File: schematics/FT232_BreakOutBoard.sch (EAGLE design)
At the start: 22 parts, among them IC1 FT232RL, X1 USB-B-S

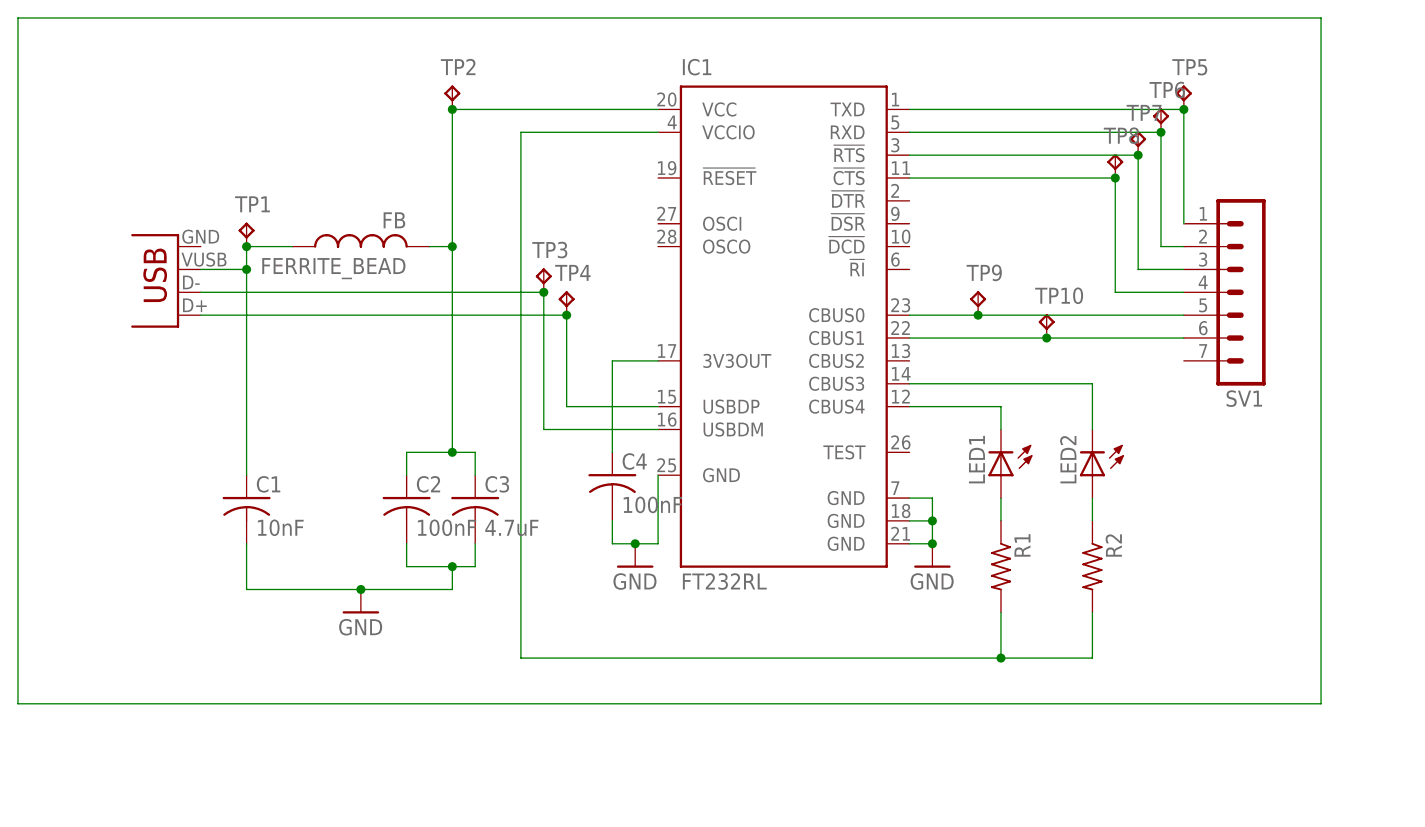
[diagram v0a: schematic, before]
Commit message: updated breakout board layout and schematic
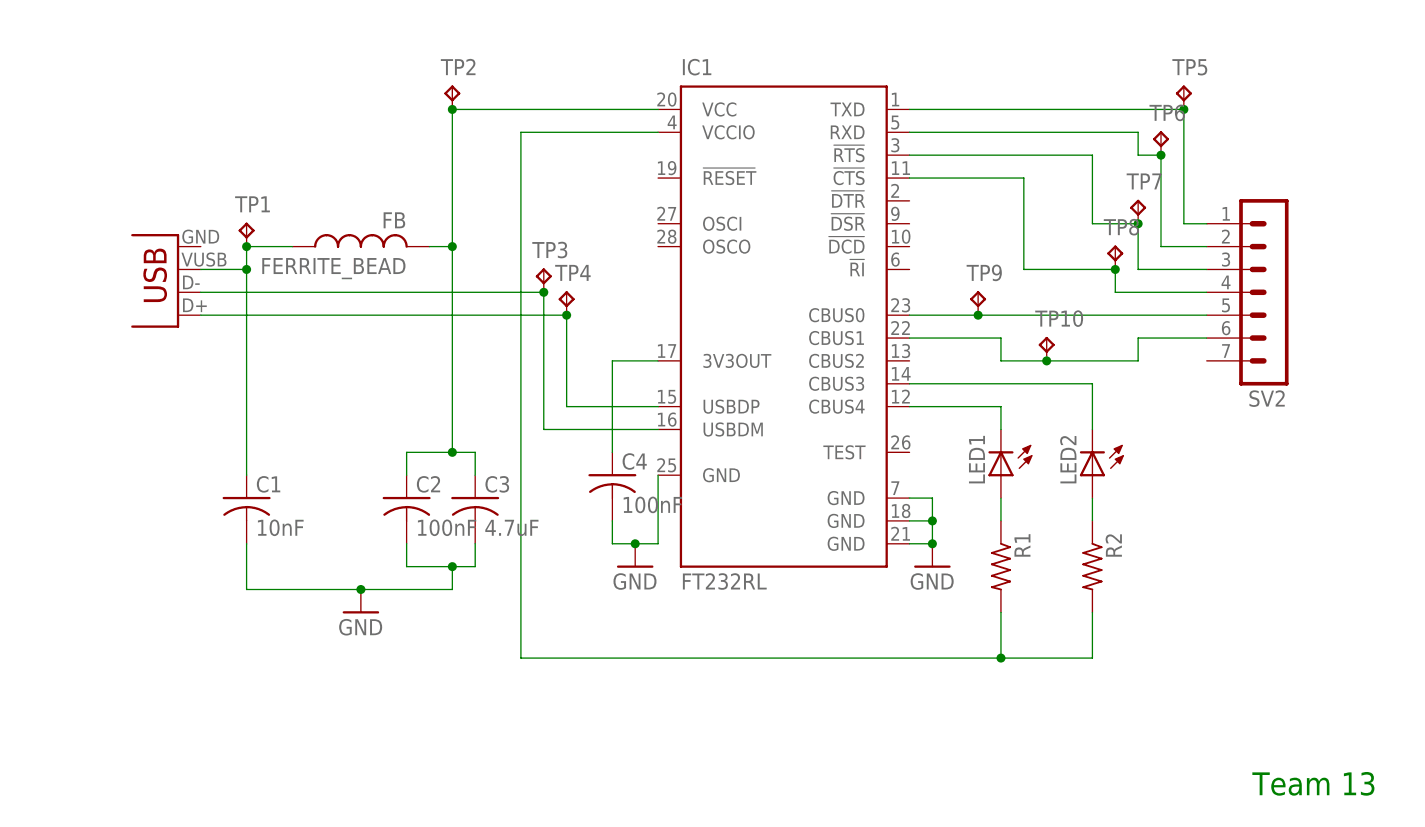
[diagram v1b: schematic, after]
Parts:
- removed SV1: (no value), con-lstb:MA07-1
- added SV2: (no value), con-lstb:MA07-1
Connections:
- net N$10: now also SV2.4; no longer SV1.4
- net N$11: now also SV2.5; no longer SV1.5
- net N$14: now also SV2.6; no longer SV1.6
- net N$6: now also SV2.1; no longer SV1.1
- net N$8: now also SV2.2
- net N$9: now also SV2.3; no longer SV1.3
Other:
- note added: "Team 13"
- moved on the sheet: TP10, TP6, TP7, TP8
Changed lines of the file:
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@@
 <?xml version="1.0" encoding="utf-8"?>
 <!DOCTYPE eagle SYSTEM "eagle.dtd">
-<eagle version="7.3.0">
+<eagle version="8.4.0">
 <drawing>
 <settings>
 <setting alwaysvectorfont="no"/>
+<setting keepoldvectorfont="yes"/>
 <setting verticaltext="up"/>
 </settings>
@@
 <layers>
 <layer number="1" name="Top" color="4" fill="1" visible="no" active="no"/>
+<layer number="2" name="Route2" color="1" fill="3" visible="no" active="no"/>
+<layer number="3" name="Route3" color="4" fill="3" visible="no" active="no"/>
+<layer number="4" name="Route4" color="1" fill="4" visible="no" active="no"/>
+<layer number="5" name="Route5" color="4" fill="4" visible="no" active="no"/>
+<layer number="6" name="Route6" color="1" fill="8" visible="no" active="no"/>
+<layer number="7" name="Route7" color="4" fill="8" visible="no" active="no"/>
+<layer number="8" name="Route8" color="1" fill="2" visible="no" active="no"/>
+<layer number="9" name="Route9" color="4" fill="2" visible="no" active="no"/>
+<layer number="10" name="Route10" color="1" fill="7" visible="no" active="no"/>
+<layer number="11" name="Route11" color="4" fill="7" visible="no" active="no"/>
+<layer number="12" name="Route12" color="1" fill="5" visible="no" active="no"/>
+<layer number="13" name="Route13" color="4" fill="5" visible="no" active="no"/>
+<layer number="14" name="Route14" color="1" fill="6" visible="no" active="no"/>
+<layer number="15" name="Route15" color="4" fill="6" visible="no" active="no"/>
 <layer number="16" name="Bottom" color="1" fill="1" visible="no" active="no"/>
 <layer number="17" name="Pads" color="2" fill="1" visible="no" active="no"/>
@@
 <part name="IC1" library="ftdichip" deviceset="FT232R" device="L"/>
 <part name="X1" library="con-usb" deviceset="USB" device="-B-S"/>
-<part name="SV1" library="con-lstb" deviceset="MA07-1" device=""/>
 <part name="LED1" library="adafruit" deviceset="LED" device="CHIPLED_0805"/>
 <part name="LED2" library="adafruit" deviceset="LED" device="CHIPLED_0805"/>
@@
 <part name="TP9" library="testpad" deviceset="TP" device="B1,27"/>
 <part name="TP10" library="testpad" deviceset="TP" device="B1,27"/>
+<part name="SV2" library="con-lstb" library_urn="urn:adsk.eagle:library:162" deviceset="MA07-1" device="" package3d_urn="urn:adsk.eagle:package:8341/1"/>
+<part name="FRAME1" library="frames" library_urn="urn:adsk.eagle:library:229" deviceset="DINA5_L" device=""/>
 </parts>
 <sheets>
 <sheet>
 <plain>
+<text x="129.54" y="25.4" size="2.54" layer="91">Team 13</text>
 </plain>
 <instances>
 <instance part="IC1" gate="1" x="76.2" y="78.74"/>
 <instance part="X1" gate="G$1" x="10.16" y="86.36" rot="R180"/>
-<instance part="SV1" gate="1" x="129.54" y="81.28" rot="R180"/>
 <instance part="LED1" gate="G$1" x="101.6" y="60.96" rot="R180"/>
 <instance part="LED2" gate="G$1" x="111.76" y="60.96" rot="R180"/>
@@
 <instance part="TP4" gate="G$1" x="53.34" y="81.28"/>
 <instance part="TP5" gate="G$1" x="121.92" y="104.14"/>
-<instance part="TP6" gate="G$1" x="119.38" y="101.6"/>
-<instance part="TP7" gate="G$1" x="116.84" y="99.06"/>
-<instance part="TP8" gate="G$1" x="114.3" y="96.52"/>
+<instance part="TP6" gate="G$1" x="119.38" y="99.06"/>
+<instance part="TP7" gate="G$1" x="116.84" y="91.44"/>
+<instance part="TP8" gate="G$1" x="114.3" y="86.36"/>
 <instance part="TP9" gate="G$1" x="99.06" y="81.28"/>
-<instance part="TP10" gate="G$1" x="106.68" y="78.74"/>
+<instance part="TP10" gate="G$1" x="106.68" y="76.2"/>
+<instance part="SV2" gate="1" x="132.08" y="81.28" rot="R180"/>
+<instance part="FRAME1" gate="G$1" x="-22.86" y="5.08"/>
 </instances>
 <busses>
 </busses>
 <nets>
-<net name="N$1" class="0">
-<segment>
-<wire x1="-7.62" y1="111.76" x2="137.16" y2="111.76" width="0.1524" layer="91"/>
-<wire x1="137.16" y1="111.76" x2="137.16" y2="35.56" width="0.1524" layer="91"/>
-<wire x1="137.16" y1="35.56" x2="-7.62" y2="35.56" width="0.1524" layer="91"/>
-<wire x1="-7.62" y1="35.56" x2="-7.62" y2="111.76" width="0.1524" layer="91"/>
-</segment>
-</net>
 <net name="N$3" class="0">
 <segment>
@@
 <segment>
 <pinref part="IC1" gate="1" pin="TXD"/>
-<pinref part="SV1" gate="1" pin="1"/>
 <wire x1="91.44" y1="101.6" x2="121.92" y2="101.6" width="0.1524" layer="91"/>
 <wire x1="121.92" y1="101.6" x2="121.92" y2="88.9" width="0.1524" layer="91"/>
 <pinref part="TP5" gate="G$1" pin="TP"/>
 <junction x="121.92" y="101.6"/>
+<pinref part="SV2" gate="1" pin="1"/>
+<wire x1="124.46" y1="88.9" x2="121.92" y2="88.9" width="0.1524" layer="91"/>
 </segment>
 </net>
@@
 <segment>
 <pinref part="IC1" gate="1" pin="RXD"/>
-<wire x1="91.44" y1="99.06" x2="119.38" y2="99.06" width="0.1524" layer="91"/>
-<wire x1="119.38" y1="99.06" x2="119.38" y2="86.36" width="0.1524" layer="91"/>
-<wire x1="119.38" y1="86.36" x2="121.92" y2="86.36" width="0.1524" layer="91"/>
+<wire x1="91.44" y1="99.06" x2="116.84" y2="99.06" width="0.1524" layer="91"/>
+<wire x1="116.84" y1="99.06" x2="116.84" y2="96.52" width="0.1524" layer="91"/>
+<wire x1="116.84" y1="96.52" x2="119.38" y2="96.52" width="0.1524" layer="91"/>
+<wire x1="119.38" y1="96.52" x2="119.38" y2="86.36" width="0.1524" layer="91"/>
 <pinref part="TP6" gate="G$1" pin="TP"/>
-<junction x="119.38" y="99.06"/>
+<junction x="119.38" y="96.52"/>
+<pinref part="SV2" gate="1" pin="2"/>
+<wire x1="124.46" y1="86.36" x2="119.38" y2="86.36" width="0.1524" layer="91"/>
 </segment>
 </net>
@@
 <segment>
 <pinref part="IC1" gate="1" pin="!RTS"/>
-<wire x1="91.44" y1="96.52" x2="116.84" y2="96.52" width="0.1524" layer="91"/>
-<wire x1="116.84" y1="96.52" x2="116.84" y2="83.82" width="0.1524" layer="91"/>
-<pinref part="SV1" gate="1" pin="3"/>
-<wire x1="116.84" y1="83.82" x2="121.92" y2="83.82" width="0.1524" layer="91"/>
+<wire x1="91.44" y1="96.52" x2="111.76" y2="96.52" width="0.1524" layer="91"/>
+<wire x1="111.76" y1="96.52" x2="111.76" y2="88.9" width="0.1524" layer="91"/>
+<wire x1="111.76" y1="88.9" x2="116.84" y2="88.9" width="0.1524" layer="91"/>
+<wire x1="116.84" y1="88.9" x2="116.84" y2="83.82" width="0.1524" layer="91"/>
+<wire x1="116.84" y1="83.82" x2="124.46" y2="83.82" width="0.1524" layer="91"/>
 <pinref part="TP7" gate="G$1" pin="TP"/>
-<junction x="116.84" y="96.52"/>
+<junction x="116.84" y="88.9"/>
+<pinref part="SV2" gate="1" pin="3"/>
 </segment>
 </net>
 <net name="N$10" class="0">
 <segment>
-<pinref part="SV1" gate="1" pin="4"/>
-<wire x1="121.92" y1="81.28" x2="114.3" y2="81.28" width="0.1524" layer="91"/>
-<wire x1="114.3" y1="81.28" x2="114.3" y2="93.98" width="0.1524" layer="91"/>
+<wire x1="124.46" y1="81.28" x2="114.3" y2="81.28" width="0.1524" layer="91"/>
+<wire x1="114.3" y1="81.28" x2="114.3" y2="83.82" width="0.1524" layer="91"/>
 <pinref part="IC1" gate="1" pin="!CTS"/>
-<wire x1="114.3" y1="93.98" x2="91.44" y2="93.98" width="0.1524" layer="91"/>
+<wire x1="114.3" y1="83.82" x2="104.14" y2="83.82" width="0.1524" layer="91"/>
+<wire x1="104.14" y1="83.82" x2="104.14" y2="93.98" width="0.1524" layer="91"/>
+<wire x1="104.14" y1="93.98" x2="91.44" y2="93.98" width="0.1524" layer="91"/>
 <pinref part="TP8" gate="G$1" pin="TP"/>
-<junction x="114.3" y="93.98"/>
+<junction x="114.3" y="83.82"/>
+<pinref part="SV2" gate="1" pin="4"/>
 </segment>
 </net>
@@
 <segment>
 <pinref part="IC1" gate="1" pin="CBUS0"/>
-<pinref part="SV1" gate="1" pin="5"/>
 <wire x1="91.44" y1="78.74" x2="99.06" y2="78.74" width="0.1524" layer="91"/>
 <pinref part="TP9" gate="G$1" pin="TP"/>
-<wire x1="99.06" y1="78.74" x2="121.92" y2="78.74" width="0.1524" layer="91"/>
+<wire x1="99.06" y1="78.74" x2="124.46" y2="78.74" width="0.1524" layer="91"/>
 <junction x="99.06" y="78.74"/>
+<pinref part="SV2" gate="1" pin="5"/>
 </segment>
 </net>
@@
 <segment>
 <pinref part="IC1" gate="1" pin="CBUS1"/>
-<pinref part="SV1" gate="1" pin="6"/>
-<wire x1="91.44" y1="76.2" x2="106.68" y2="76.2" width="0.1524" layer="91"/>
+<wire x1="91.44" y1="76.2" x2="101.6" y2="76.2" width="0.1524" layer="91"/>
+<wire x1="101.6" y1="76.2" x2="101.6" y2="73.66" width="0.1524" layer="91"/>
+<wire x1="101.6" y1="73.66" x2="106.68" y2="73.66" width="0.1524" layer="91"/>
 <pinref part="TP10" gate="G$1" pin="TP"/>
-<wire x1="106.68" y1="76.2" x2="121.92" y2="76.2" width="0.1524" layer="91"/>
-<junction x="106.68" y="76.2"/>
+<wire x1="106.68" y1="73.66" x2="116.84" y2="73.66" width="0.1524" layer="91"/>
+<wire x1="116.84" y1="73.66" x2="116.84" y2="76.2" width="0.1524" layer="91"/>
+<wire x1="116.84" y1="76.2" x2="124.46" y2="76.2" width="0.1524" layer="91"/>
+<junction x="106.68" y="73.66"/>
+<pinref part="SV2" gate="1" pin="6"/>
 </segment>
 </net>
@@
 </schematic>
 </drawing>
+<compatibility>
+<note version="8.2" severity="warning">
+Since Version 8.2, EAGLE supports online libraries. The ids
+of those online libraries will not be understood (or retained)
+with this version.
+</note>
+<note version="8.3" severity="warning">
+Since Version 8.3, EAGLE supports URNs for individual library
+assets (packages, symbols, and devices). The URNs of those assets
+will not be understood (or retained) with this version.
+</note>
+<note version="8.3" severity="warning">
+Since Version 8.3, EAGLE supports the association of 3D packages
+with devices in libraries, schematics, and board files. Those 3D
+packages will not be understood (or retained) with this version.
+</note>
+</compatibility>
 </eagle>

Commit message: Updated FT232 break-out board with corrected USB connector and larger vias
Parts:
- added C5: 100nF, adafruit:C-USC0805
- X1: value USB-B-S -> USB-B-H; device con-usb:USB-B-S -> con-usb:USB-B-H
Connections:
- new net N$1: C5.1, X1.GND
- net GND: now also C5.2
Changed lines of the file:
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@@
 <layer number="59" name="tCarbon" color="7" fill="1" visible="no" active="no"/>
 <layer number="60" name="bCarbon" color="7" fill="1" visible="no" active="no"/>
+<layer number="88" name="SimResults" color="9" fill="1" visible="yes" active="yes"/>
+<layer number="89" name="SimProbes" color="9" fill="1" visible="yes" active="yes"/>
 <layer number="90" name="Modules" color="5" fill="1" visible="yes" active="yes"/>
 <layer number="91" name="Nets" color="2" fill="1" visible="yes" active="yes"/>
@@
 <parts>
 <part name="IC1" library="ftdichip" deviceset="FT232R" device="L"/>
-<part name="X1" library="con-usb" deviceset="USB" device="-B-S"/>
 <part name="LED1" library="adafruit" deviceset="LED" device="CHIPLED_0805"/>
 <part name="LED2" library="adafruit" deviceset="LED" device="CHIPLED_0805"/>
@@
 <part name="SV2" library="con-lstb" library_urn="urn:adsk.eagle:library:162" deviceset="MA07-1" device="" package3d_urn="urn:adsk.eagle:package:8341/1"/>
 <part name="FRAME1" library="frames" library_urn="urn:adsk.eagle:library:229" deviceset="DINA5_L" device=""/>
+<part name="X1" library="con-usb" deviceset="USB" device="-B-H"/>
+<part name="C5" library="adafruit" deviceset="C-US" device="C0805" value="100nF"/>
+<part name="GND4" library="supply1" deviceset="GND" device=""/>
 </parts>
 <sheets>
@@
 <instances>
 <instance part="IC1" gate="1" x="76.2" y="78.74"/>
-<instance part="X1" gate="G$1" x="10.16" y="86.36" rot="R180"/>
 <instance part="LED1" gate="G$1" x="101.6" y="60.96" rot="R180"/>
 <instance part="LED2" gate="G$1" x="111.76" y="60.96" rot="R180"/>
@@
 <instance part="SV2" gate="1" x="132.08" y="81.28" rot="R180"/>
 <instance part="FRAME1" gate="G$1" x="-22.86" y="5.08"/>
+<instance part="X1" gate="G$1" x="10.16" y="86.36" rot="R180"/>
+<instance part="C5" gate="G$1" x="12.7" y="93.98" smashed="yes" rot="R180">
+<attribute name="NAME" x="11.684" y="93.345" size="1.778" layer="95" rot="R180"/>
+<attribute name="VALUE" x="11.684" y="98.171" size="1.778" layer="96" rot="R180"/>
+</instance>
+<instance part="GND4" gate="1" x="-2.54" y="96.52"/>
 </instances>
 <busses>
@@
 <net name="N$3" class="0">
 <segment>
-<pinref part="X1" gate="G$1" pin="D+"/>
 <wire x1="12.7" y1="78.74" x2="53.34" y2="78.74" width="0.1524" layer="91"/>
 <wire x1="53.34" y1="78.74" x2="53.34" y2="68.58" width="0.1524" layer="91"/>
@@
 <pinref part="TP4" gate="G$1" pin="TP"/>
 <junction x="53.34" y="78.74"/>
+<pinref part="X1" gate="G$1" pin="D+"/>
 </segment>
 </net>
 <net name="N$5" class="0">
 <segment>
-<pinref part="X1" gate="G$1" pin="D-"/>
 <wire x1="12.7" y1="81.28" x2="50.8" y2="81.28" width="0.1524" layer="91"/>
 <wire x1="50.8" y1="81.28" x2="50.8" y2="66.04" width="0.1524" layer="91"/>
@@
 <pinref part="TP3" gate="G$1" pin="TP"/>
 <junction x="50.8" y="81.28"/>
+<pinref part="X1" gate="G$1" pin="D-"/>
 </segment>
 </net>
 <net name="N$7" class="0">
 <segment>
-<pinref part="X1" gate="G$1" pin="VBUS"/>
 <wire x1="12.7" y1="83.82" x2="17.78" y2="83.82" width="0.1524" layer="91"/>
 <pinref part="C1" gate="G$1" pin="1"/>
@@
 <pinref part="TP1" gate="G$1" pin="TP"/>
 <junction x="17.78" y="86.36"/>
+<pinref part="X1" gate="G$1" pin="VBUS"/>
 </segment>
 </net>
@@
 <junction x="93.98" y="53.34"/>
 <pinref part="GND3" gate="1" pin="GND"/>
+</segment>
+<segment>
+<pinref part="C5" gate="G$1" pin="2"/>
+<wire x1="12.7" y1="99.06" x2="12.7" y2="104.14" width="0.1524" layer="91"/>
+<pinref part="GND4" gate="1" pin="GND"/>
+<wire x1="12.7" y1="104.14" x2="-2.54" y2="104.14" width="0.1524" layer="91"/>
+<wire x1="-2.54" y1="104.14" x2="-2.54" y2="99.06" width="0.1524" layer="91"/>
 </segment>
 </net>
@@
 </segment>
 </net>
+<net name="N$1" class="0">
+<segment>
+<pinref part="X1" gate="G$1" pin="GND"/>
+<pinref part="C5" gate="G$1" pin="1"/>
+<wire x1="12.7" y1="86.36" x2="12.7" y2="91.44" width="0.1524" layer="91"/>
+</segment>
+</net>
